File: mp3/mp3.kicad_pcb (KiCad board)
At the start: 2 copper layers, 26.9 x 53.5 mm, 33 parts, among them J1 USB4105-GF-A, J2 LEFT, J3 DEBUG, J4 RIGHT, U1 W25Q128JV, U2 RP2040, U3 MCP1702T-3302E_CB, Y1 12MHz

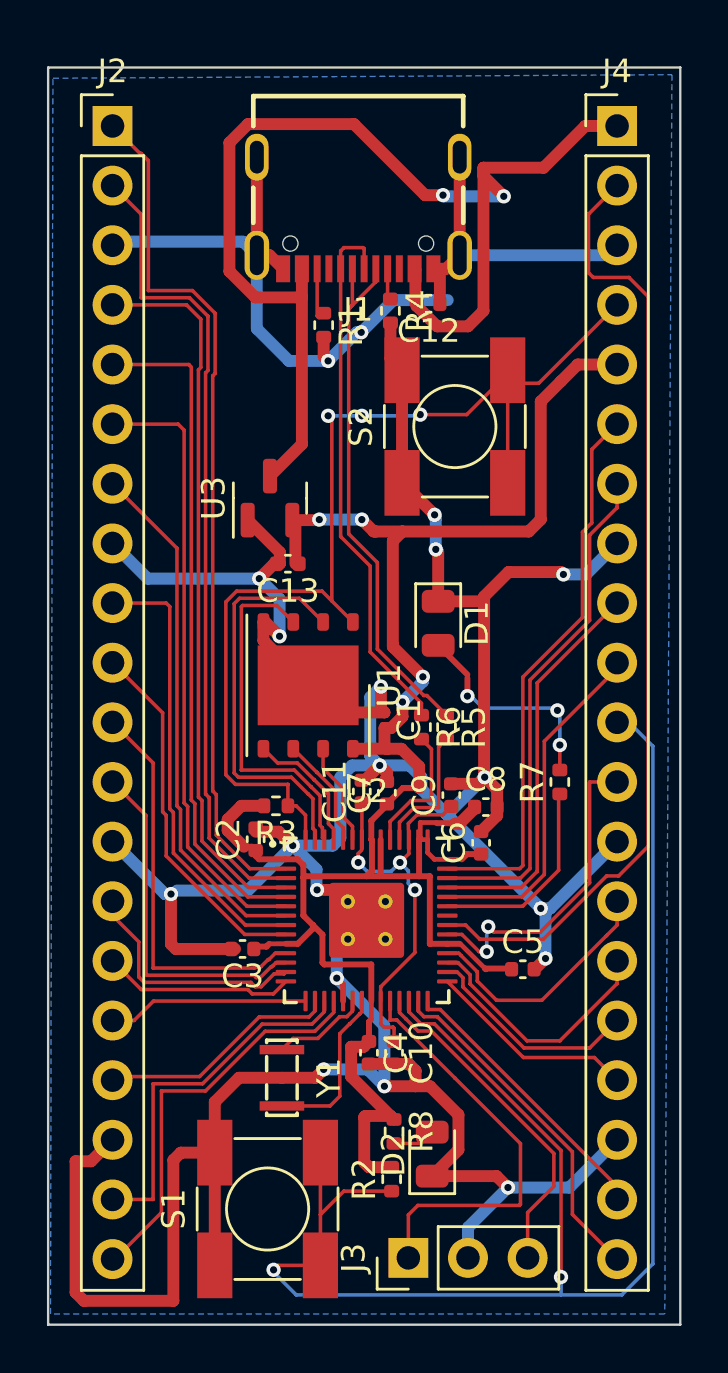
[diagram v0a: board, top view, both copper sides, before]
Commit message: Update new layout design according to Brad
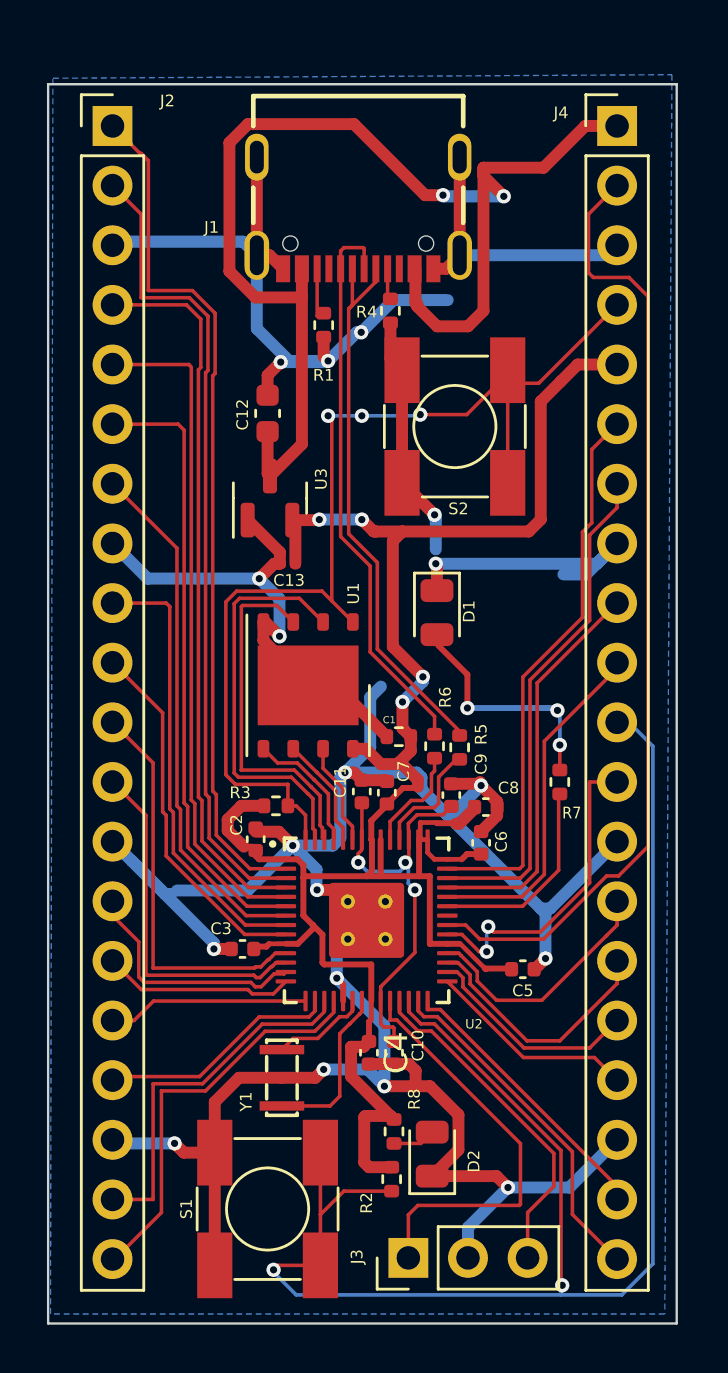
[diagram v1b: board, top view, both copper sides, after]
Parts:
- C1: footprint Resistor_SMD:R_0201_0603Metric -> Resistor_SMD:R_0402_1005Metric
- C12: footprint Capacitor_SMD:C_0402_1005Metric -> Capacitor_SMD:C_0603_1608Metric
- C13: footprint Capacitor_SMD:C_0402_1005Metric -> Capacitor_SMD:C_0201_0603Metric
- moved C12 8.30 mm to (63.2, 64.7), turned to -90 degrees
- moved R5 1.03 mm to (71.4, 78.9)
- moved R6 0.99 mm to (70.4, 78.9)
- moved C1 0.94 mm to (68.8, 78.5), turned to 0 degrees
- moved D1 0.46 mm to (70.5, 73.2)
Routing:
- net GND: track 212.7 -> 195.9 mm, vias 19 -> 18
- net /VBUS: track 50.9 -> 52.6 mm
- net Net-(J1-PadA6): track 23.1 -> 24.2 mm
- net Net-(J1-PadA7): track 23.1 -> 24.1 mm
- net Net-(R6-Pad2): track 5.70 -> 4.74 mm
- net Net-(R5-Pad2): track 5.72 -> 5.07 mm
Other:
- board size 26.9 x 53.5 mm -> 26.8 x 52.8 mm

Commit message: Make changes on layout according to Brad
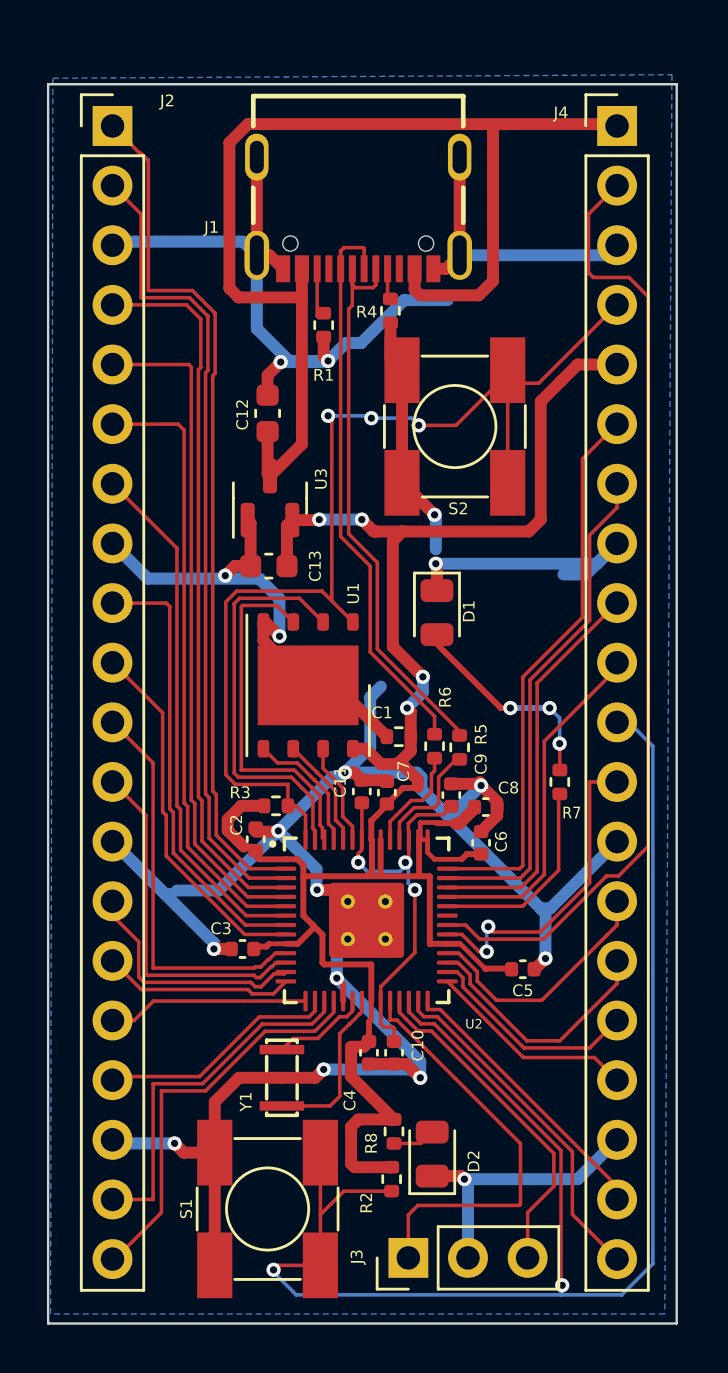
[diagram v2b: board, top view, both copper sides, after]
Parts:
- C13: footprint Capacitor_SMD:C_0201_0603Metric -> Capacitor_SMD:C_0603_1608Metric
- moved C13 0.82 mm to (63.3, 71.2)
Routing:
- net GND: track 195.9 -> 188.1 mm, vias 18 -> 17
- net /VBUS: track 52.6 -> 48.7 mm, vias 2 -> 0
- net Net-(D1-Pad2): track 9.64 -> 8.67 mm
- net +3V3: track 92.5 -> 93.4 mm
